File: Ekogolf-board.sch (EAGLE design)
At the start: 10 parts

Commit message: first routing
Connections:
- removed net N$2: SV2.6
- net N$1: no longer X2-1.KL
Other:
- moved on the sheet: X2-1, X2-2, X2-3
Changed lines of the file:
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@@
 <attribute name="NAME" x="50.8" y="69.469" size="1.778" layer="95" rot="R180"/>
 </instance>
-<instance part="X2" gate="-1" x="2.54" y="43.18" smashed="yes">
-<attribute name="NAME" x="2.54" y="44.069" size="1.778" layer="95" rot="R180"/>
+<instance part="X2" gate="-1" x="81.28" y="27.94" smashed="yes" rot="R180">
+<attribute name="NAME" x="81.28" y="27.051" size="1.778" layer="95"/>
 </instance>
-<instance part="X2" gate="-2" x="2.54" y="38.1" smashed="yes">
-<attribute name="NAME" x="2.54" y="38.989" size="1.778" layer="95" rot="R180"/>
+<instance part="X2" gate="-2" x="81.28" y="22.86" smashed="yes" rot="R180">
+<attribute name="NAME" x="81.28" y="21.971" size="1.778" layer="95"/>
 </instance>
-<instance part="X2" gate="-3" x="2.54" y="33.02" smashed="yes">
-<attribute name="VALUE" x="0" y="29.337" size="1.778" layer="96"/>
-<attribute name="NAME" x="2.54" y="33.909" size="1.778" layer="95" rot="R180"/>
+<instance part="X2" gate="-3" x="81.28" y="17.78" smashed="yes" rot="R180">
+<attribute name="VALUE" x="83.82" y="21.463" size="1.778" layer="96" rot="R180"/>
+<attribute name="NAME" x="81.28" y="16.891" size="1.778" layer="95"/>
 </instance>
 </instances>
@@
 <wire x1="35.56" y1="48.26" x2="35.56" y2="83.82" width="0.1524" layer="91"/>
 <junction x="35.56" y="83.82"/>
-<junction x="35.56" y="48.26"/>
-<pinref part="X2" gate="-1" pin="KL"/>
-<wire x1="7.62" y1="43.18" x2="17.78" y2="43.18" width="0.1524" layer="91"/>
-<wire x1="17.78" y1="43.18" x2="17.78" y2="35.56" width="0.1524" layer="91"/>
-<wire x1="17.78" y1="35.56" x2="35.56" y2="35.56" width="0.1524" layer="91"/>
-<wire x1="35.56" y1="35.56" x2="35.56" y2="48.26" width="0.1524" layer="91"/>
 </segment>
 </net>
@@
 <junction x="43.18" y="66.04"/>
 <pinref part="X2" gate="-3" pin="KL"/>
-<wire x1="7.62" y1="33.02" x2="43.18" y2="33.02" width="0.1524" layer="91"/>
+<wire x1="76.2" y1="17.78" x2="43.18" y2="33.02" width="0.1524" layer="91"/>
 <wire x1="43.18" y1="33.02" x2="43.18" y2="50.8" width="0.1524" layer="91"/>
 <junction x="43.18" y="50.8"/>
 </segment>
 </net>
-<net name="N$2" class="0">
-<segment>
-<pinref part="SV2" gate="1" pin="6"/>
-<wire x1="27.94" y1="25.4" x2="40.64" y2="25.4" width="0.1524" layer="91"/>
-</segment>
-</net>

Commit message: Poligono de Masa a GND
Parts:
- removed X2: (no value), con-wago-500:W237-103
- added LED1: TLLY4400, led:TLLY4400
- added R1: (no value), rcl:R-US_0204/5
- X1: device con-wago-500:W237-102 -> con-wago-500:W237-4
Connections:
- removed net N$3: SV1.6, X2-3.KL, X6-4.KL, X7-4.KL
- new net GND: LED1.C, SV1.6, X1-4.KL, X6-4.KL, X7-4.KL
- new net N$10: SV6.5, X1-2.KL
- new net N$5: SV6.4, X7-3.KL
- new net N$6: SV6.3, X7-2.KL
- new net N$7: SV6.2, X6-3.KL
- new net N$9: SV6.6, X1-3.KL
- new net TX3: SV6.1, X6-2.KL
- new net VCC: R1.2, SV1.5, X1-1.KL, X6-1.KL, X7-1.KL
- net N$1: now also LED1.A, R1.1; no longer SV1.5, X6-1.KL, X7-1.KL
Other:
- moved on the sheet: X1-1, X1-2

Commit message: somo titles
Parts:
- renumbered LED1 to INDEX, R1 to 330, X1 to T3, X6 to T1, X7 to T2
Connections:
- net GND: now also SV1.7

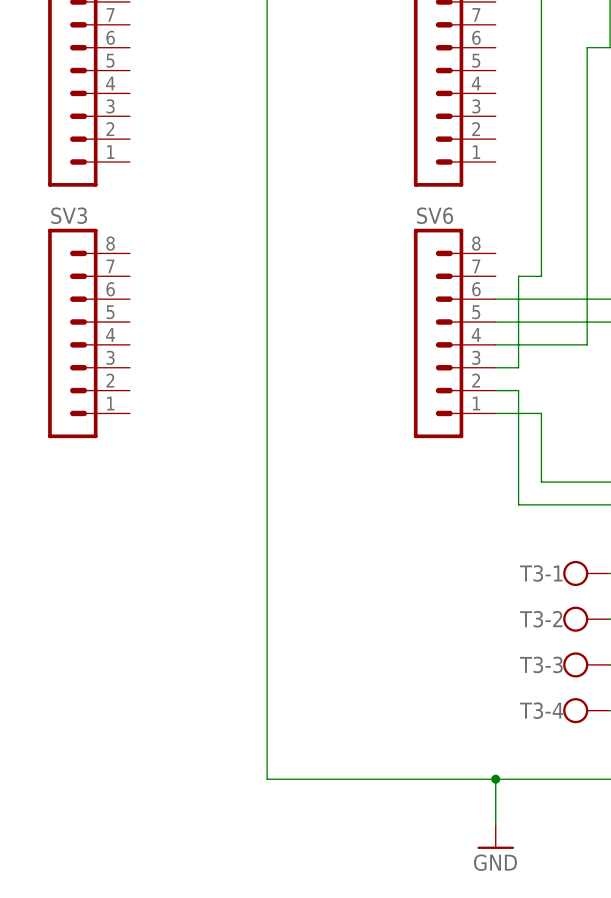
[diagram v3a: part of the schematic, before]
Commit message: se agrega led indicador
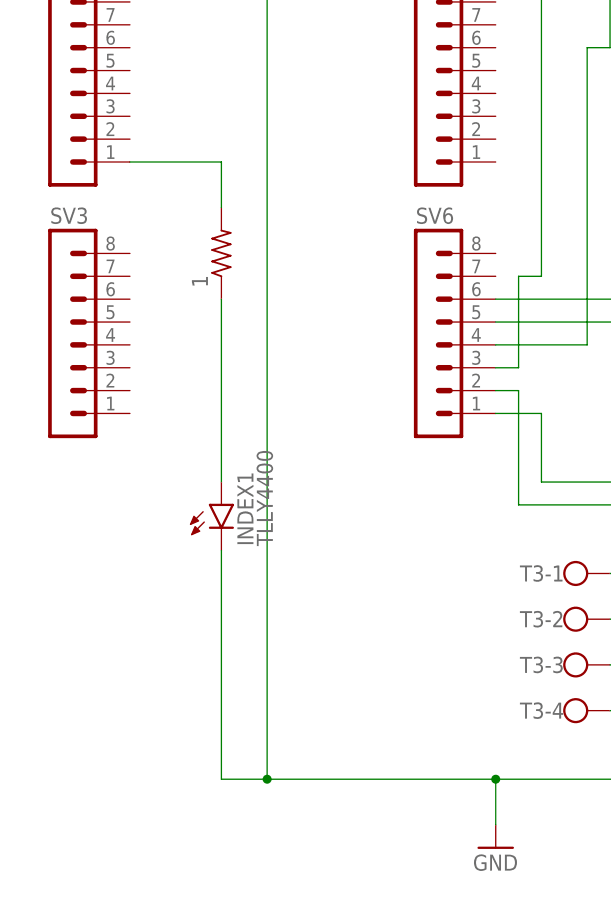
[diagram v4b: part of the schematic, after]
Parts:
- added 1: (no value), rcl:R-US_0204/5
- added INDEX1: TLLY4400, led:TLLY4400
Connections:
- new net N$2: 1.2, SV2.1
- new net N$3: 1.1, INDEX1.A
- net GND: now also INDEX1.C
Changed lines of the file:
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@@
 <part name="330" library="rcl" library_urn="urn:adsk.eagle:library:334" deviceset="R-US_" device="0204/5" package3d_urn="urn:adsk.eagle:package:23488/1"/>
 <part name="INDEX" library="led" library_urn="urn:adsk.eagle:library:259" deviceset="TLLY4400" device="" package3d_urn="urn:adsk.eagle:package:15797/1"/>
+<part name="1" library="rcl" library_urn="urn:adsk.eagle:library:334" deviceset="R-US_" device="0204/5" package3d_urn="urn:adsk.eagle:package:23488/1"/>
+<part name="INDEX1" library="led" library_urn="urn:adsk.eagle:library:259" deviceset="TLLY4400" device="" package3d_urn="urn:adsk.eagle:package:15797/1"/>
 </parts>
 <sheets>
@@
 <attribute name="NAME" x="128.016" y="-55.372" size="1.778" layer="95" rot="R90"/>
 <attribute name="VALUE" x="130.175" y="-55.372" size="1.778" layer="96" rot="R90"/>
+</instance>
+<instance part="1" gate="G$1" x="38.1" y="2.54" smashed="yes" rot="R90">
+<attribute name="NAME" x="36.6014" y="-1.27" size="1.778" layer="95" rot="R90"/>
+<attribute name="VALUE" x="41.402" y="-1.27" size="1.778" layer="96" rot="R90"/>
+</instance>
+<instance part="INDEX1" gate="G$1" x="38.1" y="-25.4" smashed="yes">
+<attribute name="NAME" x="41.656" y="-29.972" size="1.778" layer="95" rot="R90"/>
+<attribute name="VALUE" x="43.815" y="-29.972" size="1.778" layer="96" rot="R90"/>
 </instance>
 </instances>
@@
 <wire x1="27.94" y1="53.34" x2="43.18" y2="53.34" width="0.1524" layer="91"/>
 <junction x="43.18" y="53.34"/>
+<pinref part="INDEX1" gate="G$1" pin="C"/>
+<wire x1="38.1" y1="-30.48" x2="38.1" y2="-55.88" width="0.1524" layer="91"/>
+<wire x1="38.1" y1="-55.88" x2="43.18" y2="-55.88" width="0.1524" layer="91"/>
+<junction x="43.18" y="-55.88"/>
 </segment>
 </net>
@@
 </segment>
 </net>
+<net name="N$2" class="0">
+<segment>
+<pinref part="SV2" gate="1" pin="1"/>
+<pinref part="1" gate="G$1" pin="2"/>
+<wire x1="27.94" y1="12.7" x2="38.1" y2="12.7" width="0.1524" layer="91"/>
+<wire x1="38.1" y1="12.7" x2="38.1" y2="7.62" width="0.1524" layer="91"/>
+</segment>
+</net>
+<net name="N$3" class="0">
+<segment>
+<pinref part="INDEX1" gate="G$1" pin="A"/>
+<pinref part="1" gate="G$1" pin="1"/>
+<wire x1="38.1" y1="-22.86" x2="38.1" y2="-2.54" width="0.1524" layer="91"/>
+</segment>
+</net>
